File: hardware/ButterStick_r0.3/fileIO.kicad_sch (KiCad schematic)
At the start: 2 parts, among them J2 MicroSD, U3 PUSB3FR6

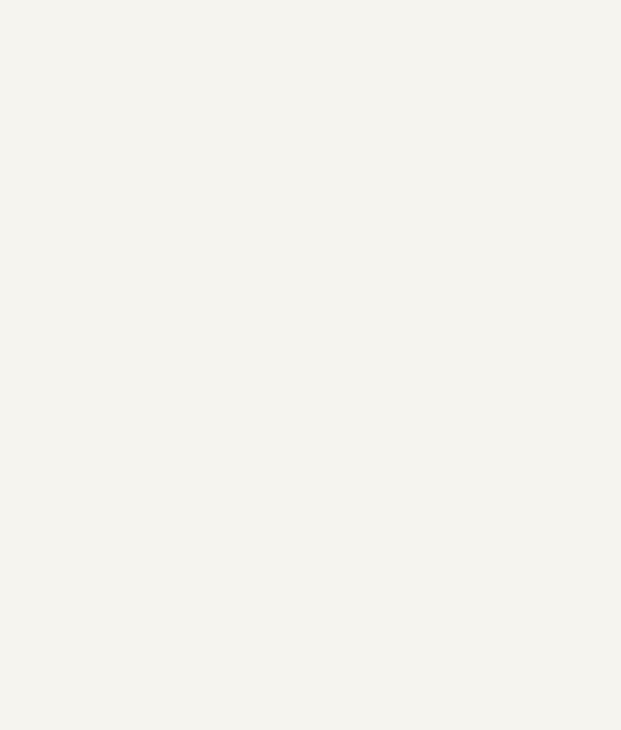
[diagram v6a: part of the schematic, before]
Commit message: hw.r0d3: Continue routing
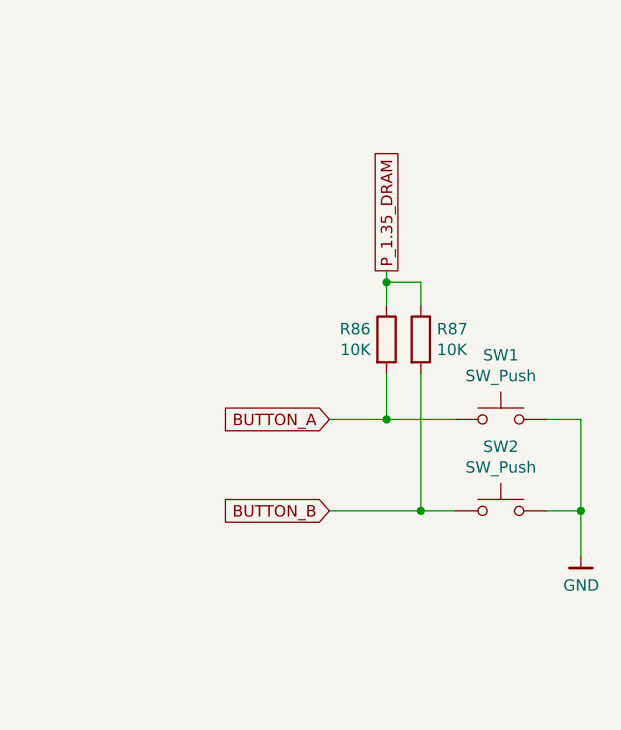
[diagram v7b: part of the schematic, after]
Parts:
- added R86, R87: 10K, Resistor_SMD:R_0402_1005Metric, symbol Device:R
- added SW1, SW2: SW_Push, Button_Switch_SMD:SW_SPST_PTS810, symbol Switch:SW_Push
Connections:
- net GND: now also SW1.2, SW2.2
- new net BUTTON_A: R86.2, SW1.1
- new net BUTTON_B: R87.2, SW2.1
- new net P_1.35_DRAM: R86.1, R87.1
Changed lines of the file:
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@@
 (kicad_sch (version 20200608) (host eeschema "5.99.0-unknown-08c61e6~101~ubuntu18.04.1")
-  (page 1 19)
+  (page 4 19)
   (paper "A4")
   (title_block
@@
   (junction (at 138.43 100.33))
   (junction (at 138.43 102.87))
+  (junction (at 219.71 78.74))
+  (junction (at 219.71 93.98))
+  (junction (at 223.52 104.14))
+  (junction (at 241.3 104.14))
   (junction (at 129.54 54.61))
   (bus_entry (at 134.62 57.15) (size -2.54 -2.54))
@@
     (stroke (width 0) (type solid) (color 0 0 0 0))
   )
+  (wire (pts (xy 213.36 93.98) (xy 219.71 93.98))
+    (stroke (width 0) (type solid) (color 0 0 0 0))
+  )
+  (wire (pts (xy 213.36 104.14) (xy 223.52 104.14))
+    (stroke (width 0) (type solid) (color 0 0 0 0))
+  )
+  (wire (pts (xy 219.71 77.47) (xy 219.71 78.74))
+    (stroke (width 0) (type solid) (color 0 0 0 0))
+  )
+  (wire (pts (xy 219.71 78.74) (xy 219.71 81.28))
+    (stroke (width 0) (type solid) (color 0 0 0 0))
+  )
+  (wire (pts (xy 219.71 88.9) (xy 219.71 93.98))
+    (stroke (width 0) (type solid) (color 0 0 0 0))
+  )
+  (wire (pts (xy 219.71 93.98) (xy 227.33 93.98))
+    (stroke (width 0) (type solid) (color 0 0 0 0))
+  )
+  (wire (pts (xy 223.52 78.74) (xy 219.71 78.74))
+    (stroke (width 0) (type solid) (color 0 0 0 0))
+  )
+  (wire (pts (xy 223.52 81.28) (xy 223.52 78.74))
+    (stroke (width 0) (type solid) (color 0 0 0 0))
+  )
+  (wire (pts (xy 223.52 88.9) (xy 223.52 104.14))
+    (stroke (width 0) (type solid) (color 0 0 0 0))
+  )
+  (wire (pts (xy 223.52 104.14) (xy 227.33 104.14))
+    (stroke (width 0) (type solid) (color 0 0 0 0))
+  )
+  (wire (pts (xy 237.49 104.14) (xy 241.3 104.14))
+    (stroke (width 0) (type solid) (color 0 0 0 0))
+  )
+  (wire (pts (xy 241.3 93.98) (xy 237.49 93.98))
+    (stroke (width 0) (type solid) (color 0 0 0 0))
+  )
+  (wire (pts (xy 241.3 104.14) (xy 241.3 93.98))
+    (stroke (width 0) (type solid) (color 0 0 0 0))
+  )
+  (wire (pts (xy 241.3 109.22) (xy 241.3 104.14))
+    (stroke (width 0) (type solid) (color 0 0 0 0))
+  )
   (bus (pts (xy 113.03 54.61) (xy 129.54 54.61))
     (stroke (width 0) (type solid) (color 0 0 0 0))
@@
     (effects (font (size 1.524 1.524)) (justify right))
   )
+  (global_label "BUTTON_A" (shape input) (at 213.36 93.98 180)
+    (effects (font (size 1.27 1.27)) (justify right))
+  )
+  (global_label "BUTTON_B" (shape input) (at 213.36 104.14 180)
+    (effects (font (size 1.27 1.27)) (justify right))
+  )
+  (global_label "P_1.35_DRAM" (shape passive) (at 219.71 77.47 90)
+    (effects (font (size 1.27 1.27)) (justify left))
+  )
   (hierarchical_label "{LED[0..6] LEDC[0..5]}" (shape input) (at 113.03 54.61 180)
     (effects (font (size 1.27 1.27)) (justify right))
@@
     )
   )
+  (symbol (lib_id "gkl_power:GND") (at 241.3 109.22 0) (unit 1)
+    (in_bom yes) (on_board yes)
+    (property "Reference" "#PWR0208" (id 0) (at 241.3 115.57 0)
+      (effects (font (size 1.27 1.27)) hide)
+    )
+    (property "Value" "GND" (id 1) (at 241.3381 112.4268 0))
+    (property "Footprint" "" (id 2) (at 238.76 118.11 0)
+      (effects (font (size 1.27 1.27)) hide)
+    )
+    (property "Datasheet" "" (id 3) (at 241.3 109.22 0)
+      (effects (font (size 1.27 1.27)) hide)
+    )
+  )
   (symbol (lib_id "gkl_power:+3V3") (at 138.43 74.93 0) (unit 1)
     (in_bom yes) (on_board yes)
@@
       (effects (font (size 1.27 1.27)) hide)
     )
+  )
+  (symbol (lib_id "Device:R") (at 219.71 85.09 0) (unit 1)
+    (in_bom yes) (on_board yes)
+    (property "Reference" "R86" (id 0) (at 217.9319 83.9406 0)
+      (effects (font (size 1.27 1.27)) (justify right))
+    )
+    (property "Value" "10K" (id 1) (at 217.9319 86.2393 0)
+      (effects (font (size 1.27 1.27)) (justify right))
+    )
+    (property "Footprint" "Resistor_SMD:R_0402_1005Metric" (id 2) (at 217.932 85.09 90)
+      (effects (font (size 1.27 1.27)) hide)
+    )
+    (property "Datasheet" "~" (id 3) (at 219.71 85.09 0)
+      (effects (font (size 1.27 1.27)) hide)
+    )
+  )
+  (symbol (lib_id "Device:R") (at 223.52 85.09 0) (unit 1)
+    (in_bom yes) (on_board yes)
+    (property "Reference" "R87" (id 0) (at 225.2981 83.9406 0)
+      (effects (font (size 1.27 1.27)) (justify left))
+    )
+    (property "Value" "10K" (id 1) (at 225.2981 86.2393 0)
+      (effects (font (size 1.27 1.27)) (justify left))
+    )
+    (property "Footprint" "Resistor_SMD:R_0402_1005Metric" (id 2) (at 221.742 85.09 90)
+      (effects (font (size 1.27 1.27)) hide)
+    )
+    (property "Datasheet" "~" (id 3) (at 223.52 85.09 0)
+      (effects (font (size 1.27 1.27)) hide)
+    )
+  )
+  (symbol (lib_id "Switch:SW_Push") (at 232.41 93.98 0) (unit 1)
+    (in_bom yes) (on_board yes)
+    (property "Reference" "SW1" (id 0) (at 232.41 86.8488 0))
+    (property "Value" "SW_Push" (id 1) (at 232.41 89.1475 0))
+    (property "Footprint" "Button_Switch_SMD:SW_SPST_PTS810" (id 2) (at 232.41 88.9 0)
+      (effects (font (size 1.27 1.27)) hide)
+    )
+    (property "Datasheet" "~" (id 3) (at 232.41 88.9 0)
+      (effects (font (size 1.27 1.27)) hide)
+    )
+  )
+  (symbol (lib_id "Switch:SW_Push") (at 232.41 104.14 0) (unit 1)
+    (in_bom yes) (on_board yes)
+    (property "Reference" "SW2" (id 0) (at 232.41 97.0088 0))
+    (property "Value" "SW_Push" (id 1) (at 232.41 99.3075 0))
+    (property "Footprint" "Button_Switch_SMD:SW_SPST_PTS810" (id 2) (at 232.41 99.06 0)
+      (effects (font (size 1.27 1.27)) hide)
+    )
+    (property "Datasheet" "~" (id 3) (at 232.41 99.06 0)
+      (effects (font (size 1.27 1.27)) hide)
+    )

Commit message: hw.r0d3: update DDR3 pinmap and routing
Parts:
- renumbered R86 to R33, R87 to R34
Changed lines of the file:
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@@
 (kicad_sch (version 20200608) (host eeschema "5.99.0-unknown-08c61e6~101~ubuntu18.04.1")
-  (page 4 19)
+  (page 1 19)
   (paper "A4")
   (title_block
@@
   (symbol (lib_id "gkl_power:GND") (at 241.3 109.22 0) (unit 1)
     (in_bom yes) (on_board yes)
-    (property "Reference" "#PWR0208" (id 0) (at 241.3 115.57 0)
+    (property "Reference" "#PWR058" (id 0) (at 241.3 115.57 0)
       (effects (font (size 1.27 1.27)) hide)
     )
@@
   (symbol (lib_id "Device:R") (at 219.71 85.09 0) (unit 1)
     (in_bom yes) (on_board yes)
-    (property "Reference" "R86" (id 0) (at 217.9319 83.9406 0)
+    (property "Reference" "R33" (id 0) (at 217.9319 83.9406 0)
       (effects (font (size 1.27 1.27)) (justify right))
     )
@@
   (symbol (lib_id "Device:R") (at 223.52 85.09 0) (unit 1)
     (in_bom yes) (on_board yes)
-    (property "Reference" "R87" (id 0) (at 225.2981 83.9406 0)
+    (property "Reference" "R34" (id 0) (at 225.2981 83.9406 0)
       (effects (font (size 1.27 1.27)) (justify left))
     )
